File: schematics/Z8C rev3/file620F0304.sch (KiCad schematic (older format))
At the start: 14 parts

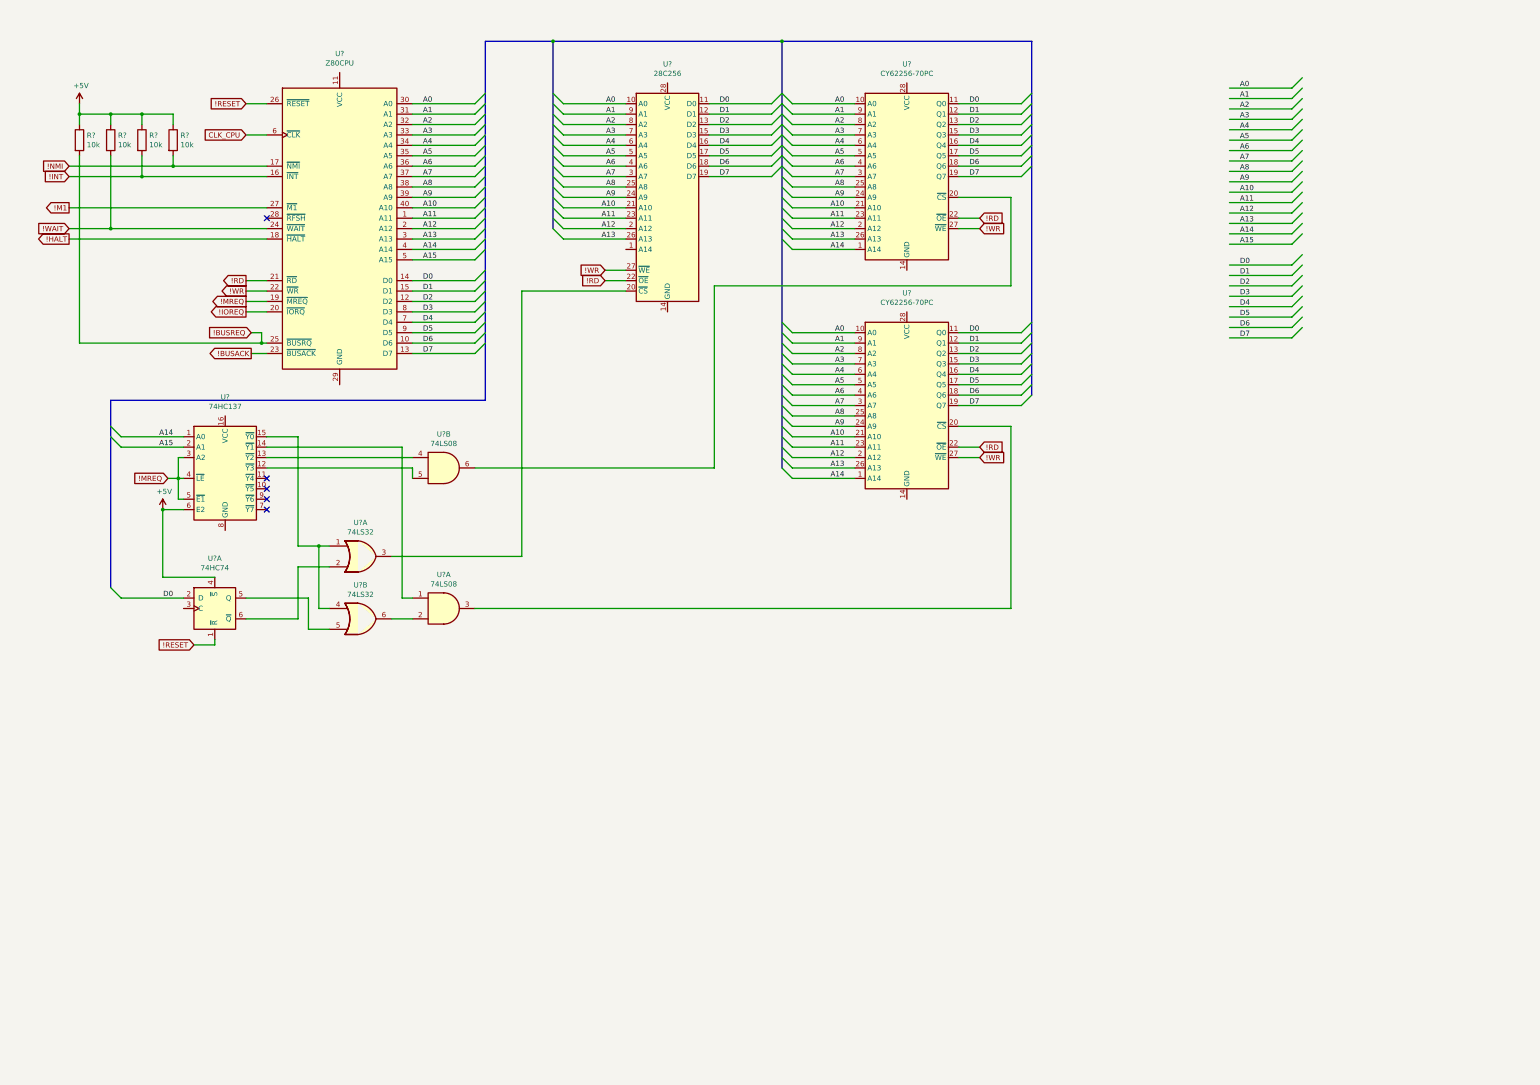
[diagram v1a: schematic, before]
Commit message: added bank switching, apu, dma and IRQ logic. Misc. improvements
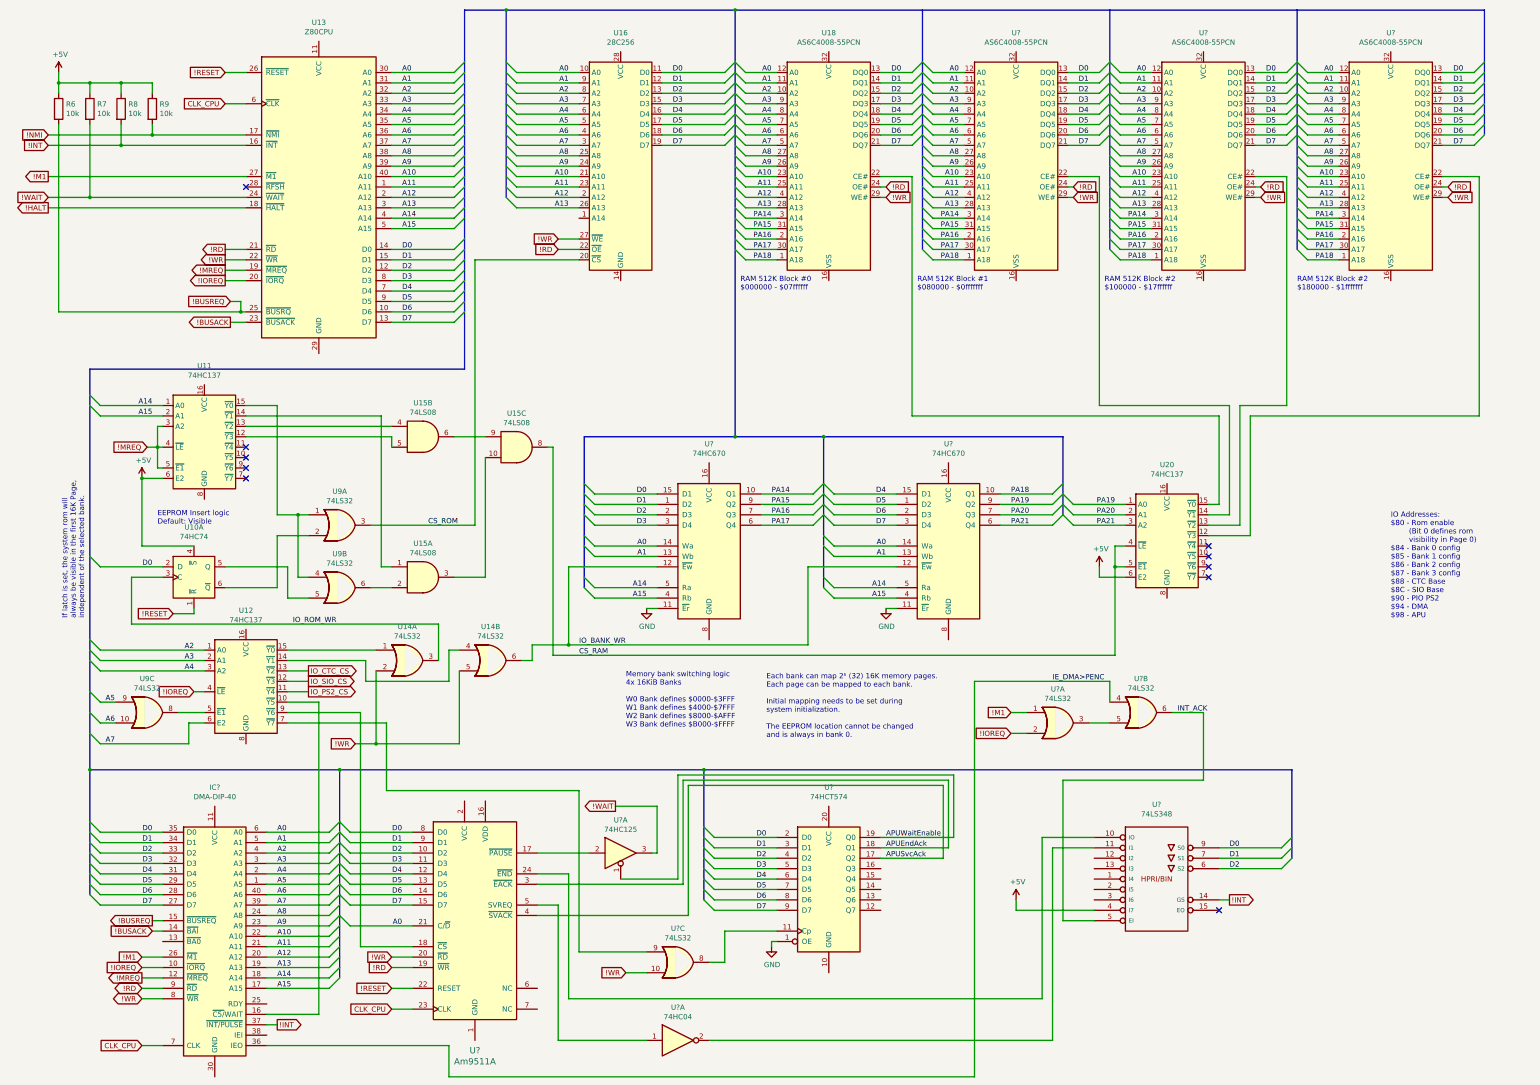
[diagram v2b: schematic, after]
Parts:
- removed U? (x2): CY62256-70PC, Package_DIP:DIP-28_W15.24mm, symbol Memory_RAM:CY62256-70PC
- added IC?: DMA-DIP-40, Package_DIP:DIP-40_W15.24mm_LongPads, symbol Zilog_Z80_Peripherals2:DMA-DIP-40
- added U12, U20: 74HC137, Package_DIP:DIP-14_W7.62mm_LongPads, symbol 74xx:74HC137
- added U14, U? (x3): 74LS32, Package_DIP:DIP-14_W7.62mm_LongPads, symbol 74xx:74LS32
- added unit 3 of U15
- added U18, U? (x3): AS6C4008-55PCN, Package_DIP:DIP-32_W15.24mm, symbol Memory_RAM:AS6C4008-55PCN
- added unit 3 of U9
- added U? (x2): 74HC670, symbol 74xx:74LS670
- added U?: Am9511A, *DIP*24*, symbol Mini8085Ext-cache:Am9511A
- added U?: 74HCT574, symbol 74xx:74HCT574
- added U?: 74HC125, Package_DIP:DIP-14_W7.62mm_LongPads, symbol 74xx:74LS125
- added U?: 74LS348, symbol 74xx_IEEE:74LS348
- added U?: 74HC04, symbol 74xx:74HC04
- U10, U11, U15, U9: renamed from U?; footprint (none) -> Package_DIP:DIP-14_W7.62mm_LongPads
- U13: renamed from U?; footprint (none) -> Package_DIP:DIP-40_W15.24mm_LongPads
- U16: renamed from U?; footprint (none) -> Package_DIP:DIP-28_W15.24mm_LongPads
- gave numbers to parts that had none: 4
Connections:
- net labels added: APUEndAck, APUSvcAck, APUWaitEnable, CS_RAM, CS_ROM, GND, IE_DMA>PENC, INT_ACK, IO_BANK_WR, IO_CTC_CS, IO_PS2_CS, IO_ROM_WR, IO_SIO_CS, PA14, PA15, PA16, PA17, PA18, PA19, PA20, PA21
- wire segments 197 -> 448
- no-connect marks 5 -> 10
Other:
- note added: "EEPROM Insert logic\nDefault: Visible"
- note added: "Each bank can map 2⁵ (32) 16K memory pages. \nEach page can be mapped to each bank.\n\nInitial mapping needs to be set during\nsystem initialization.\n\nThe EEPROM location cannot be changed\nand is always in bank 0."
- note added: "IO Addresses:\n$80 - Rom enable \n (Bit 0 defines rom \n visibility in Page 0)\n$84 - Bank 0 config\n$85 - Bank 1 config\n$86 - Bank 2 config\n$87 - Bank 3 config\n$88 - CTC Base\n$8C - SIO Base\n$90 - PIO PS2\n$94 - DMA \n$98 - APU"
- note added: "If latch is set, the system rom will \nalways be visible in the first 16K Page,\nindependent of the selected bank."
- note added: "Memory bank switching logic\n4x 16KiB Banks\n\nW0 Bank defines $0000-$3FFF\nW1 Bank defines $4000-$7FFF\nW2 Bank defines $8000-$AFFF\nW3 Bank defines $B000-$FFFF\n"
- note added: "RAM 512K Block #0\n$000000 - $07ffffff"
- note added: "RAM 512K Block #1\n$080000 - $0fffffff"
- note added: "RAM 512K Block #2\n$100000 - $17ffffff"
- note added: "RAM 512K Block #2\n$180000 - $1fffffff"
- moved on the sheet: R6, R7, R8, R9, U10A, U11, U13, U15A, U15B, U16, U9A, U9B
